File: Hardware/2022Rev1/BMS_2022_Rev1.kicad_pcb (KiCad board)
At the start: 2 copper layers, 114.3 x 124.5 mm, 105 parts, among them J1 Molex_uF_SV_03, J2 Molex_uF_SV_03, J3 Molex_uF_SV_04, J4 RJ45_LED_Shielded, J5 Molex_uF_SV_06, Q1 2N7000, Q3 2N7000, Q4 IRFS7530, SW2 SW_SP3T, U1 Teensy4.1_DEV-16771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

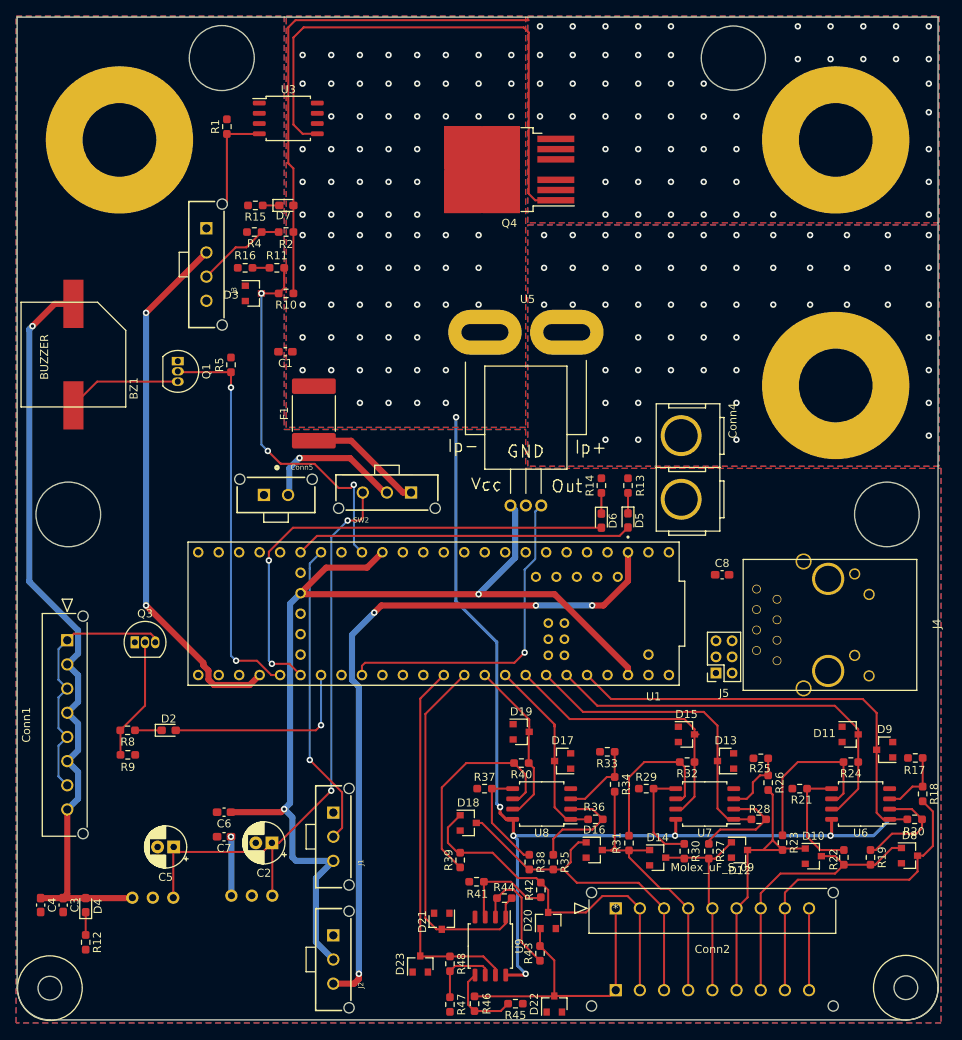
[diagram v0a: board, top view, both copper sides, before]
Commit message: minimize some wire distance
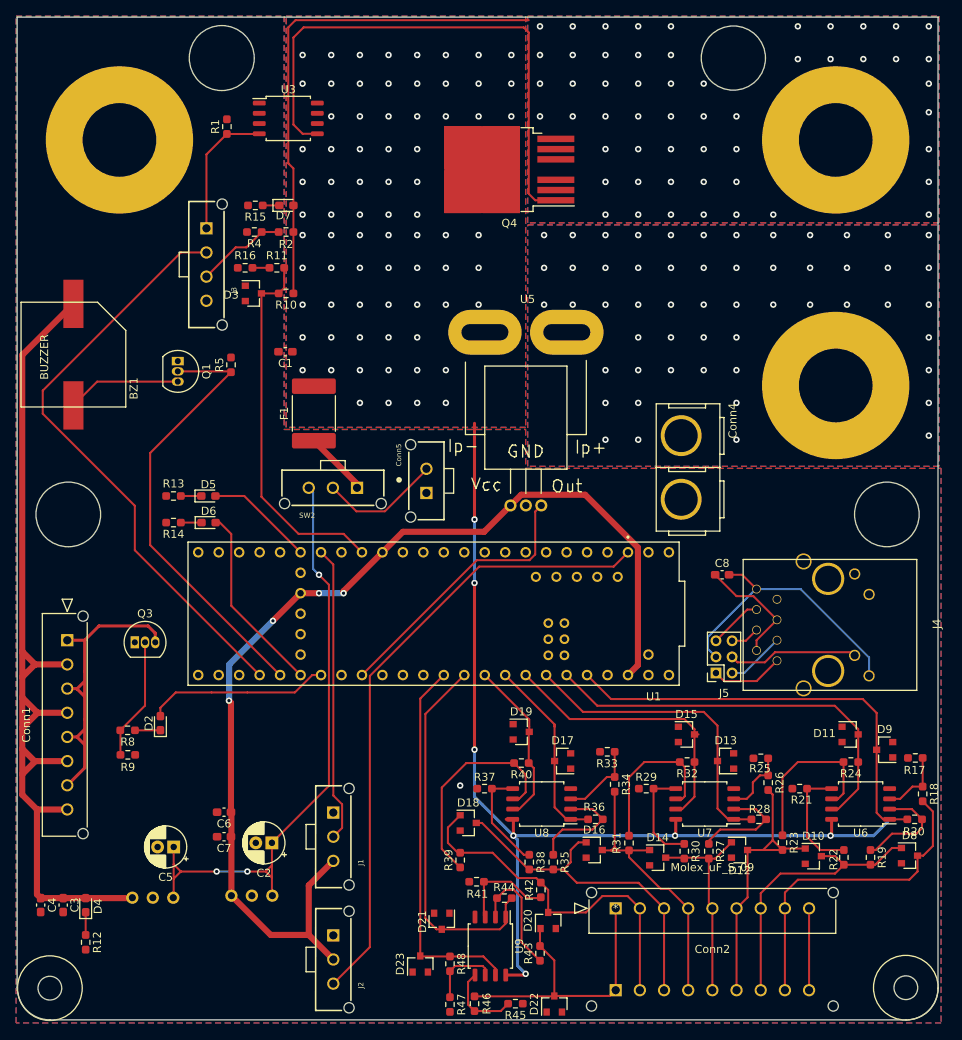
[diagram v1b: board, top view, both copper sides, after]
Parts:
- moved R13 56.4 mm to (-101.9, -240.9), turned to 180 degrees
- moved R14 53.3 mm to (-101.9, -237.6), turned to 180 degrees
- moved D5 52.2 mm to (-97.5, -240.9), turned to 0 degrees
- moved D6 48.8 mm to (-97.5, -237.6), turned to 0 degrees
- moved Conn5 18.8 mm to (-70.5, -242.8), turned to 90 degrees
- moved SW2 6.73 mm to (-82.1, -241.9)
- moved D2 1.36 mm to (-103.5, -212.7), turned to 90 degrees
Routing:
- net SW_ERR: track 60.7 -> 23.6 mm, vias 2 -> 0
- net Net-(C8-Pad2): track 0.00 -> 35.3 mm
- net SW_IND: track 41.9 -> 13.5 mm
- net +5V: track 95.4 -> 118.6 mm, vias 1 -> 0
- net Net-(J4-Pad10): track 0.00 -> 16.2 mm
- net Net-(C8-Pad1): track 0.00 -> 14.9 mm
- net Net-(J4-Pad1): track 0.00 -> 9.04 mm
- net SER_TX_IND: track 87.1 -> 78.9 mm, vias 4 -> 0
- net PACK_GATE: track 66.5 -> 73.9 mm, vias 2 -> 0
- net Net-(J4-Pad3): track 0.00 -> 7.26 mm
- net Net-(Conn1-Pad1): track 32.7 -> 39.9 mm
- net PACK_I_SENSE: track 41.1 -> 34.1 mm, vias 1 -> 0
- net Net-(F1-Pad1): track 14.7 -> 8.06 mm
- net Net-(J4-Pad6): track 0.00 -> 6.64 mm
- net BUZZER: track 48.9 -> 55.1 mm, vias 2 -> 0
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
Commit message: added some gnd vias
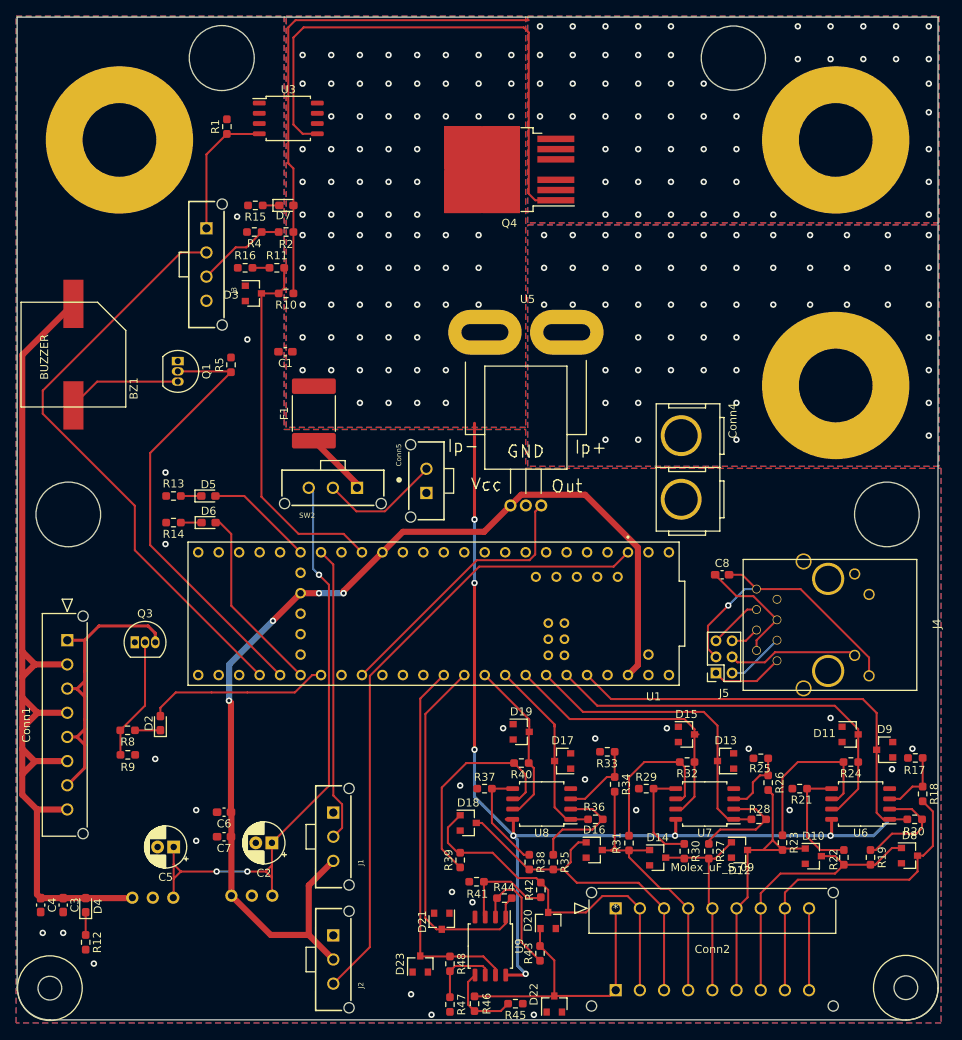
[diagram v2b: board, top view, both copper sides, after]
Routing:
- net Net-(C8-Pad2): track 35.3 -> 36.1 mm, vias 0 -> 1
- net GND: vias 1 -> 26

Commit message: fix the connector
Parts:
- added REF**: 4_40_Hole, MRDT_Drill_Holes:4_40_Hole, F.Cu at (-32.4, -295.3)
- added REF**: 4_40_Hole, MRDT_Drill_Holes:4_40_Hole, F.Cu at (-95.9, -295.3)
- added REF**: 4_40_Hole, MRDT_Drill_Holes:4_40_Hole, F.Cu at (-114.9, -238.8)
- added REF**: 4_40_Hole, MRDT_Drill_Holes:4_40_Hole, F.Cu at (-13.3, -238.8)
- Conn3: moved to F.Cu
- U2: value OKI -> 5V OKI
- U4: value OKI -> 3V3 OKI
- moved BZ1 31.3 mm to (-112.4, -283.2)
- moved V1 30.5 mm to (-108.6, -254.6)
- moved R5 18.8 mm to (-105.4, -272.7), turned to 270 degrees
- moved Q1 18.4 mm to (-112.4, -272.4), turned to 90 degrees
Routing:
- net PACK_GATE: track 73.9 -> 123.4 mm
- net +5V: track 118.6 -> 154.8 mm
- net BUZZER: track 55.1 -> 72.8 mm
- net Net-(BZ1-Pad1): track 14.2 -> 8.46 mm
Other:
- outline, holes or cut-outs redrawn
- board text added: "1 2 3 4 5 6 7 8 G"

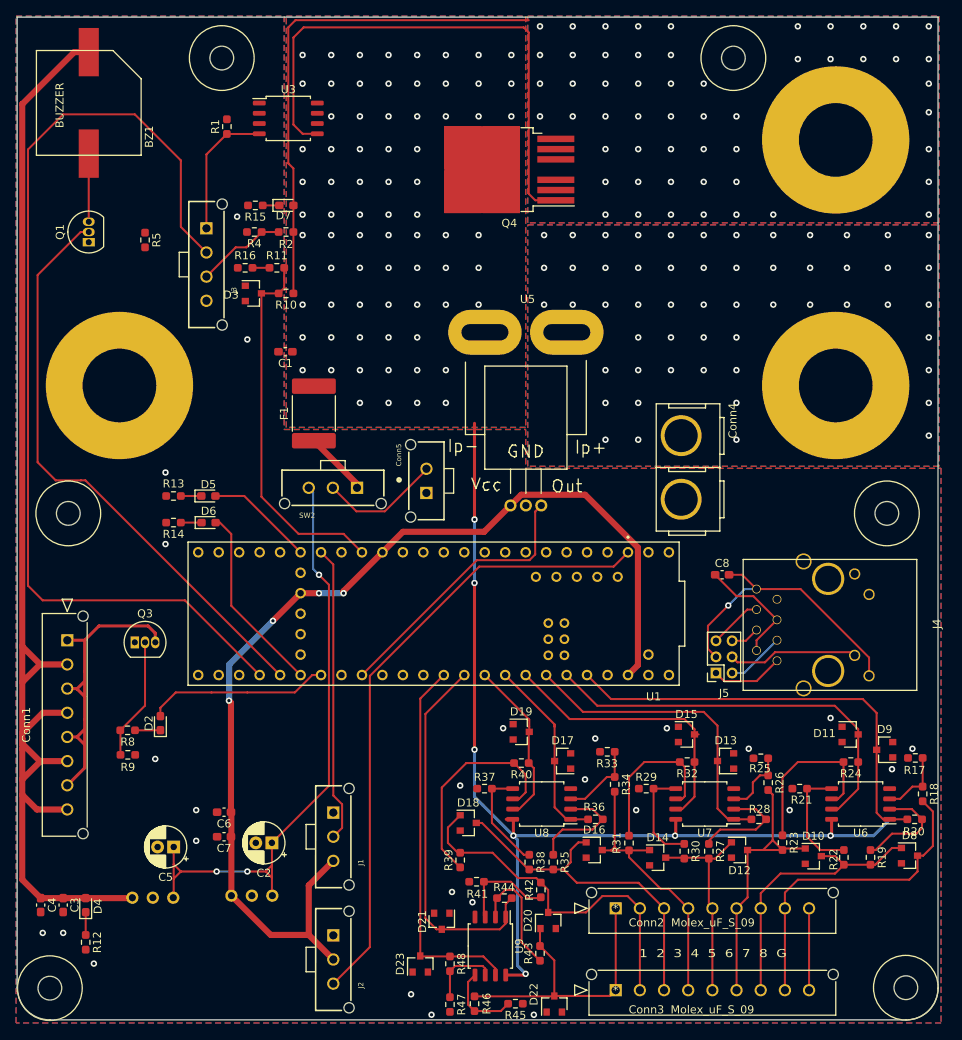
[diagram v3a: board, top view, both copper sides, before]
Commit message: Labeled connectors and moved components away from the edge of the board
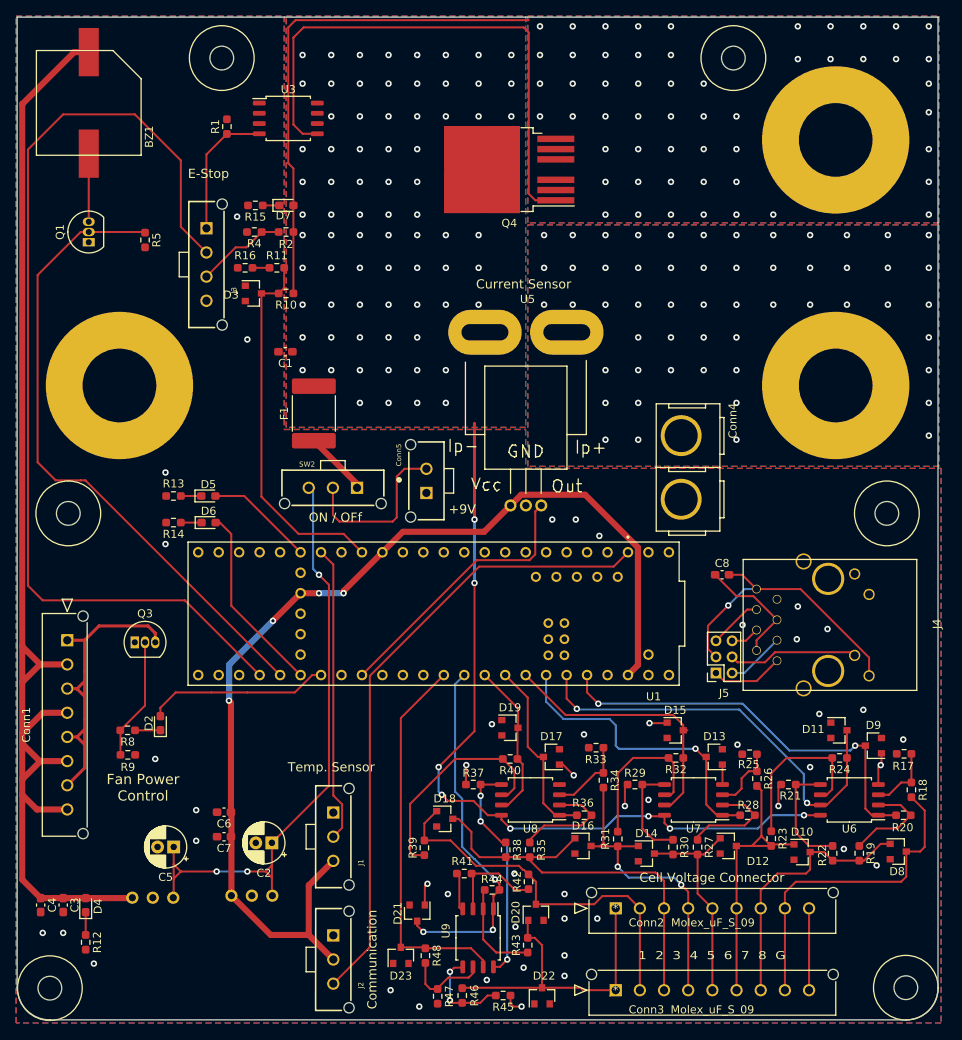
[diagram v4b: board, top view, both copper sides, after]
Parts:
- moved R39 4.70 mm to (-70.7, -197.3)
- moved R35 3.29 mm to (-57.7, -197.0)
- moved R38 3.29 mm to (-60.6, -197.0)
- moved D21 3.21 mm to (-71.6, -189.2)
- moved R48 3.21 mm to (-70.6, -183.9)
- moved D18 2.96 mm to (-68.2, -200.8)
- moved D23 2.64 mm to (-73.7, -183.9)
- moved D20 1.83 mm to (-56.9, -189.2)
- moved D22 1.83 mm to (-56.1, -178.9)
- moved R41 1.83 mm to (-65.8, -194.1)
- moved R42 1.83 mm to (-57.8, -193.0)
- moved R43 1.83 mm to (-57.9, -185.2)
- moved R44 1.83 mm to (-62.3, -192.0)
- moved R45 1.83 mm to (-61.0, -178.9)
- moved R46 1.83 mm to (-66.0, -178.9)
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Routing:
- net GND: track 10.2 -> 39.0 mm, vias 26 -> 47
- net PACK_V: track 127.8 -> 116.9 mm, vias 81 -> 83
- net CELL_3: track 43.1 -> 51.3 mm
- net BUZZER: track 72.8 -> 79.9 mm
- net Net-(Conn5-Pad2): track 15.1 -> 21.1 mm
- net CELL_4: track 35.0 -> 38.8 mm, vias 0 -> 2
- net CELL_1: track 37.1 -> 40.1 mm
- net CELL_2: track 44.4 -> 47.1 mm
- net Net-(R43-Pad1): track 15.1 -> 12.4 mm
- net CELL_8_7_SENSE: track 54.4 -> 51.9 mm, vias 0 -> 2
- net CELL_7_6_SENSE: track 50.7 -> 52.9 mm, vias 0 -> 2
- net CELL_7: track 35.8 -> 33.7 mm
- net Net-(R45-Pad2): track 9.70 -> 11.6 mm, vias 0 -> 2
- net Net-(R37-Pad2): track 13.1 -> 11.3 mm, vias 0 -> 2
- net CELL_5: track 25.6 -> 27.3 mm
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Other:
- board text added: "+9V"
- board text added: "Cell Voltage Connector"
- board text added: "Communication"
- board text added: "Current Sensor"
- board text added: "E-Stop"
- board text added: "Fan Power Control"
- board text added: "ON / OFf"
- board text added: "Temp. Sensor"

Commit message: add skills
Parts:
- added G***: LOGO, MRDT_Silkscreens:0_MRDT_Logo_10mm, B.Cu at (-77.5, -292.7)
- added G***: LOGO, MRDT_Silkscreens:z_sig_SanfanLiu_sig21.8mmx12.3mm1, B.Cu at (-50.8, -282.6)
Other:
- board text added: "5V"
- board text added: "Battery Management System, Rev 1.0 Mars Rover Design Team Missouri S&T, 2022 Sean Duda, Sanfan Liu"
- board text added: "Buzzer_SW"
- board text added: "GND"
- board text added: "SW_ERR"
- board text added: "SW_IND"
- board text added: "V_IN"
- board text added: "V_OUT"
- board text added: "V_Out"

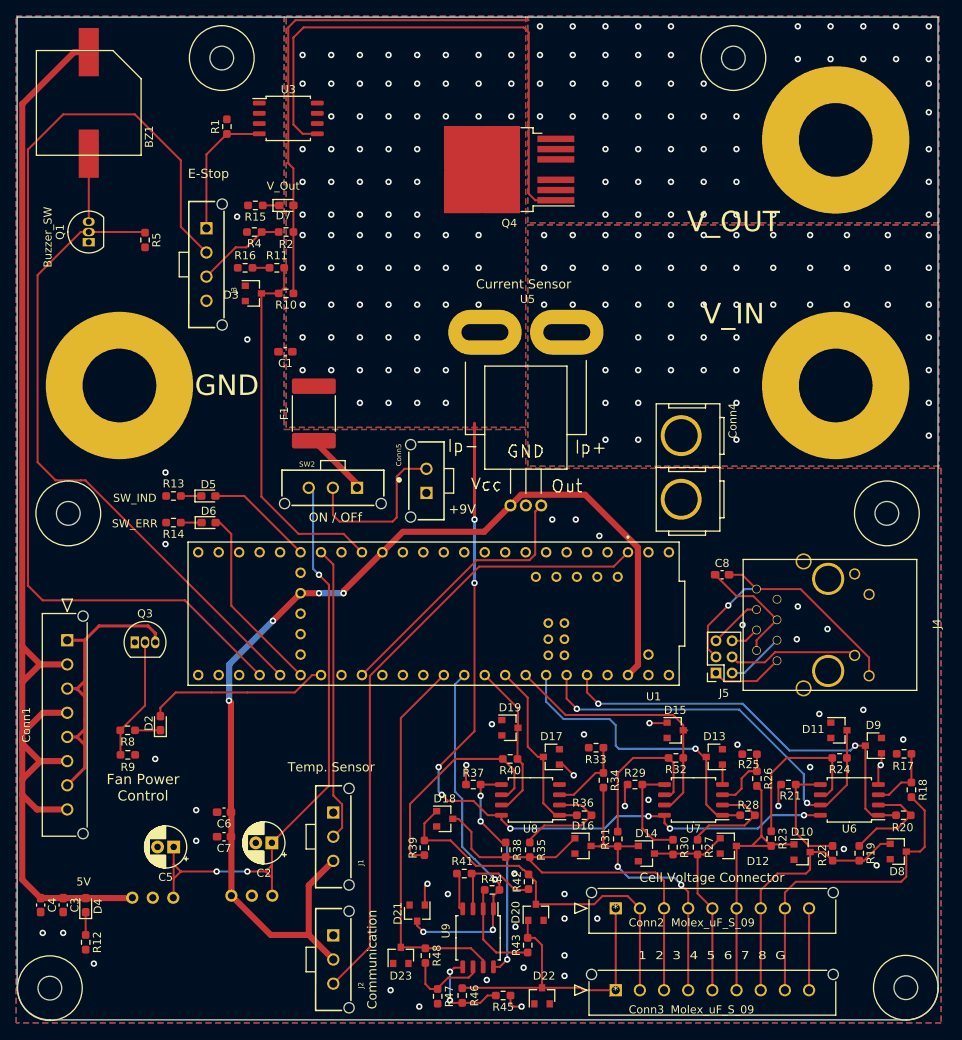
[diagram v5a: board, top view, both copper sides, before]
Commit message: Fixed differential pairing and replaced the buck
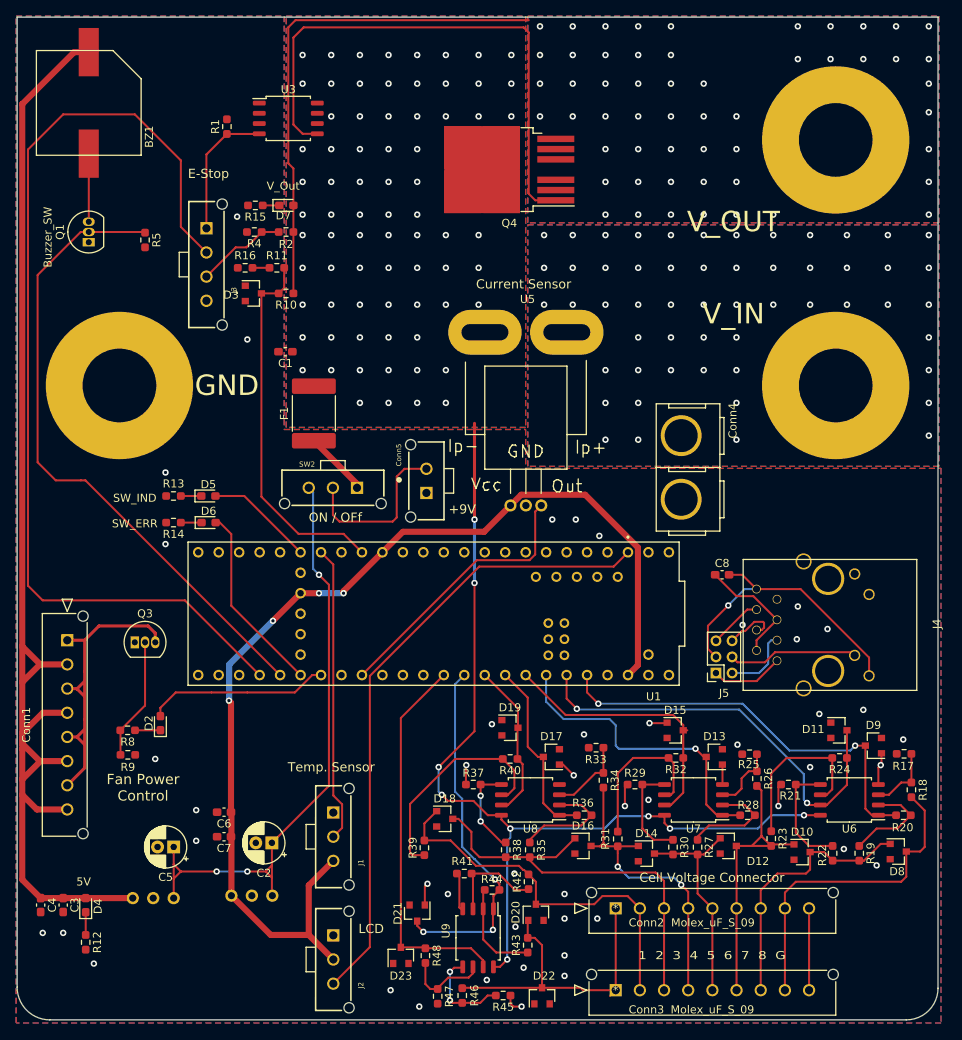
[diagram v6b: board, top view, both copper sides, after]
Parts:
- removed the G*** at (-77.5, -292.7)
- removed REF** (x4): 4_40_Hole, MRDT_Drill_Holes:4_40_Hole
- removed REF** (x2): 4_40_Hole, MRDT_Drill_Holes:4_40_Hole_Corner
- added G***: LOGO, MRDT_Silkscreens:Sean_Duda_22mmx30mm, B.Cu at (-40.6, -273.8)
- added G***: LOGO, MRDT_Silkscreens:0_MRDT_Logo_40mm, B.Cu at (-70.9, -214.1)
- U2: value 5V OKI -> OKI
- U4: value 3V3 OKI -> OKI
- moved G*** 10.4 mm to (-40.4, -283.1)
- moved U4 0.07 mm to (-101.9, -191.0)
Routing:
- net Net-(J4-Pad4): track 3.59 -> 7.07 mm
- net Net-(J4-Pad3): track 7.26 -> 9.17 mm
- net PACK_V: track 116.9 -> 118.6 mm
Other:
- board text added: "LCD"
- board text removed: "Communication"

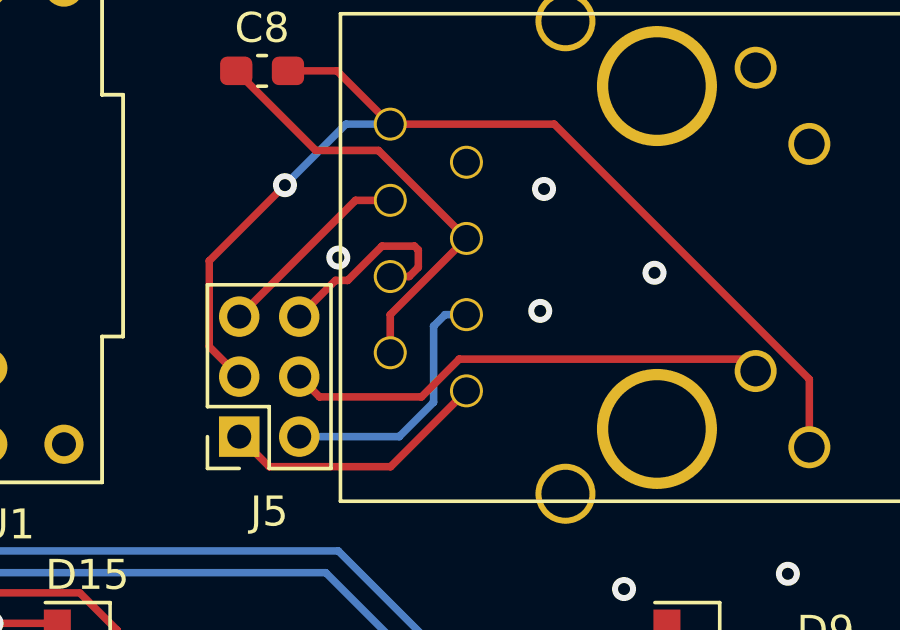
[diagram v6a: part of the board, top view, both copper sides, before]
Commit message: tweaked diff pair on pin 2 of teensy ethernet connector
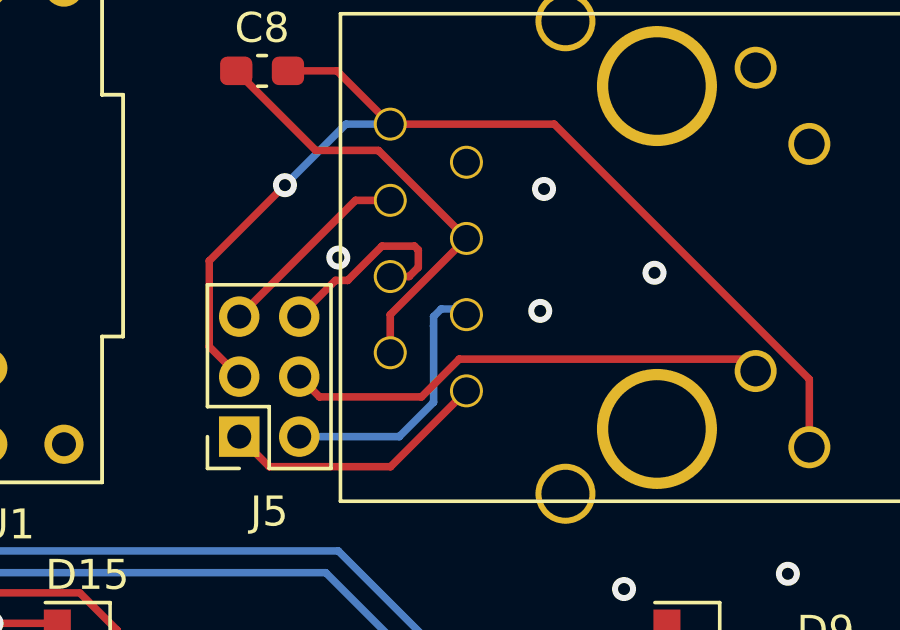
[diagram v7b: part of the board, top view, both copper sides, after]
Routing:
- net Net-(J4-Pad3): track 9.17 -> 10.7 mm
